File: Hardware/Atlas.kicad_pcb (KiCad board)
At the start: 2 copper layers, 82.5 x 70 mm, 31 parts, among them U1 MS5611, U2 HTU21D, U3 uSD Card, U4 RFD900, U5 MPU9150, U6 XBEE, U7 VENUS838LPX-L

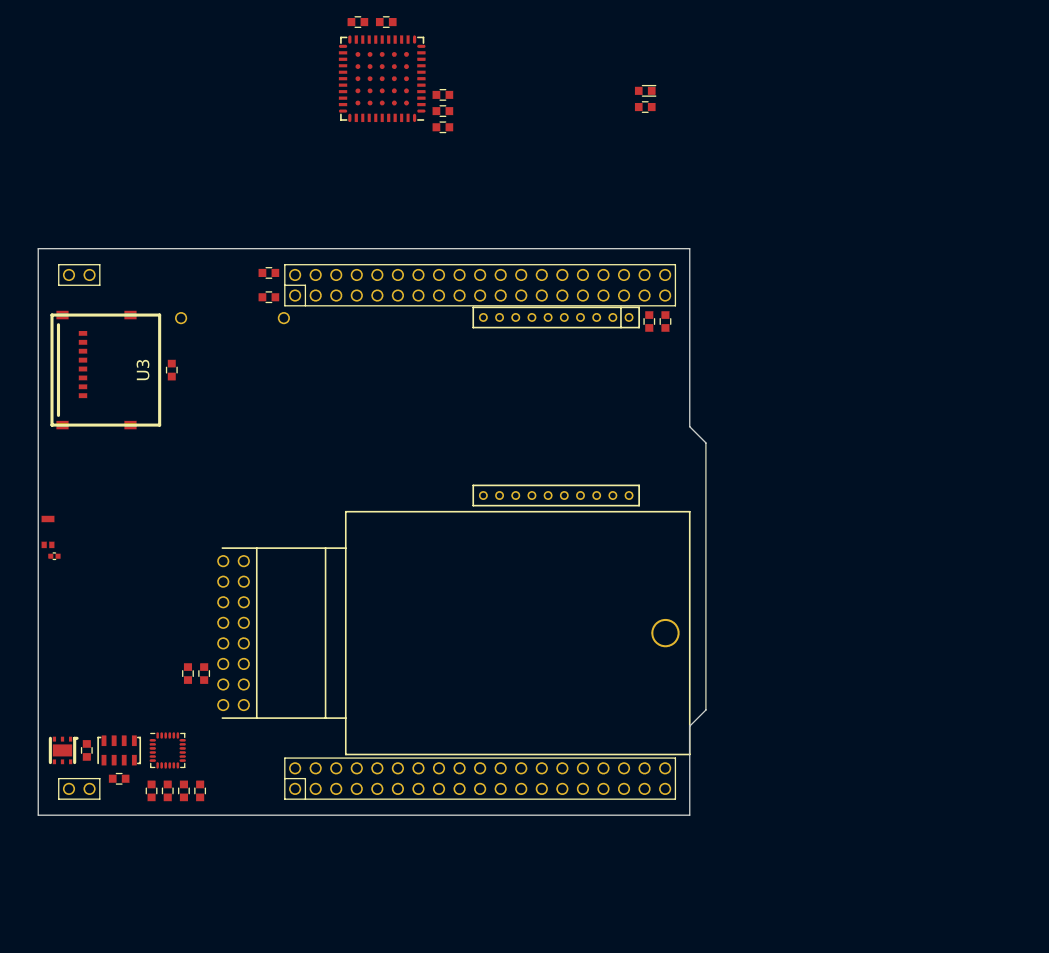
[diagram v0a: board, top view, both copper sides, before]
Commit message: Add 5v regulator and remove before flight switch
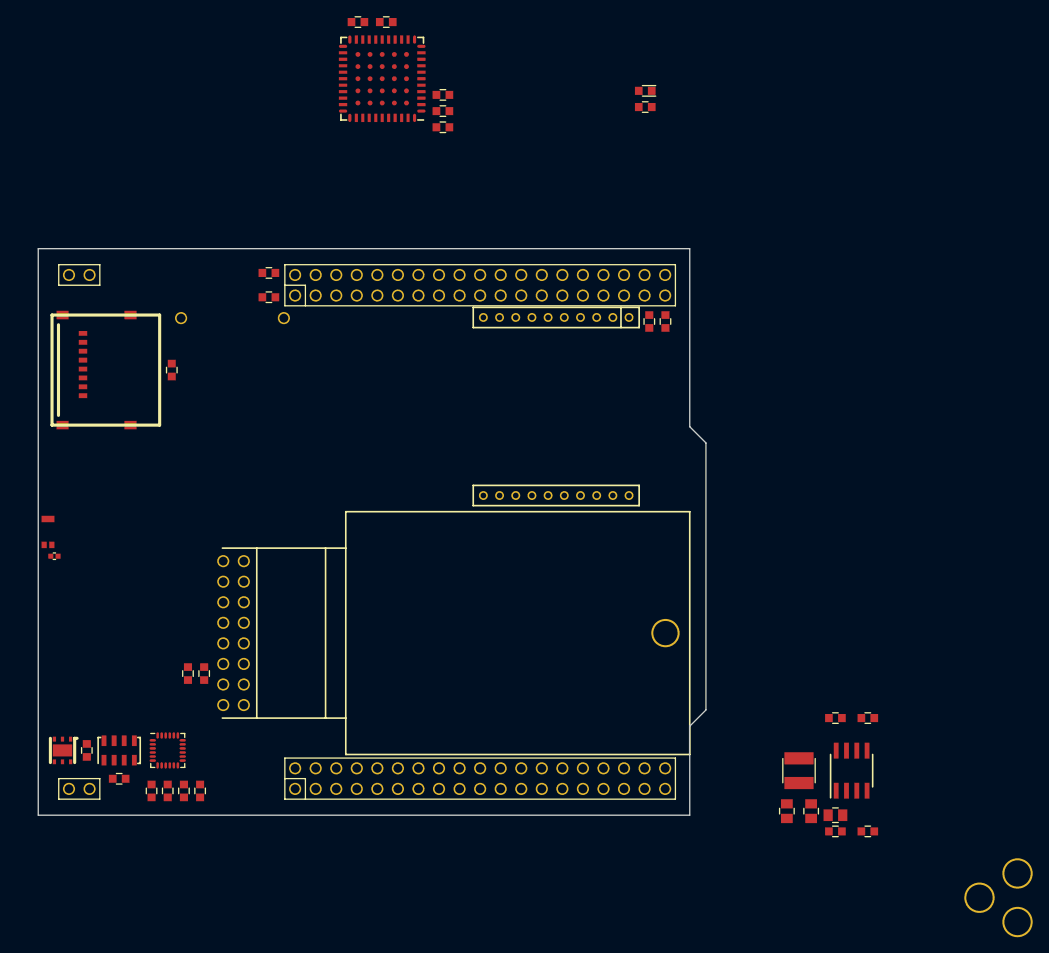
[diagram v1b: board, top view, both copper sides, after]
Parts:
- added C15: 10uF, CAPC2012-N, F.Cu at (198.5, 140.0)
- added C16: C, CAPC1608-N, F.Cu at (198.5, 128.0)
- added C17: 10uF, CAPC2012-N, F.Cu at (195.5, 139.5)
- added C18: 10uF, CAPC2012-N, F.Cu at (192.5, 139.5)
- added J1: DC, CONN-DC-CUI-202, F.Cu at (221.0, 139.5)
- added L2: 4.7uH, INDC-SRN4018, F.Cu at (194.0, 134.5)
- added R6: R, RESC1608-N, F.Cu at (202.5, 128.0)
- added R7: 52.3k, RESC1608-N, F.Cu at (198.5, 142.0)
- added R8: 10k, RESC1608-N, F.Cu at (202.5, 142.0)
- added U8: AOZ1031, SOIC127P600-8N, F.Cu at (200.5, 134.5)
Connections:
- B1 pad 1: (no net) -> +BATT
- B1 pad 2: GND -> N-0000036
- H1 pad D16: (no net) -> +3.3V
- H1 pad D18: (no net) -> +5V
- H1 pad D6: (no net) -> +5V

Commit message: Majority of layout and routing
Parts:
- removed R5: 0, RESC1608-N
- added MECH-HOLE220: VAL**, MECH-HOLE220, F.Cu at (110.0, 137.0)
- added MECH-HOLE220: VAL**, MECH-HOLE220, F.Cu at (110.0, 73.0)
- moved J1 121.5 mm to (100.0, 128.0), turned to 90 degrees
- moved R8 86.3 mm to (117.0, 130.0), turned to 270 degrees
- moved R6 86.0 mm to (117.0, 137.0), turned to 270 degrees
- moved D1 85.2 mm to (98.0, 87.0), turned to 270 degrees
- moved C16 84.0 mm to (115.0, 137.0), turned to 270 degrees
- moved R7 81.9 mm to (117.0, 133.5), turned to 270 degrees
- moved U8 79.5 mm to (121.0, 135.0), turned to 180 degrees
- moved C15 78.2 mm to (121.0, 129.5)
- moved C17 67.5 mm to (128.5, 131.0), turned to 90 degrees
- moved C18 67.5 mm to (125.5, 131.0), turned to 90 degrees
- moved L2 67.0 mm to (127.0, 136.0), turned to 90 degrees
- moved R4 66.3 mm to (122.5, 93.0), turned to 180 degrees
- moved C4 59.9 mm to (107.0, 77.5), turned to 270 degrees
- moved C2 58.5 mm to (127.0, 79.5), turned to 90 degrees
- moved C6 56.6 mm to (107.0, 81.5), turned to 270 degrees
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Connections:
- net N-0000016 renamed /LX
- AE1 pad S: AGND -> GND
- H1 pad D18: +5V -> (no net)
- H1 pad E12: (no net) -> /GOMI
- H1 pad E14: (no net) -> /GIMO
- H1 pad E21: (no net) -> /SIMO
- H1 pad E33: (no net) -> /SOMI
- H1 pad E35: (no net) -> /LIMO
- H1 pad E37: (no net) -> /LOMI
- L1 pad 1: AGND -> GND
- U4 pad 7: (no net) -> /LIMO
- U4 pad 9: (no net) -> /LOMI
- U6 pad 2: (no net) -> /SOMI
- U6 pad 3: (no net) -> /SIMO
- U7 pad 21: AGND -> GND
- U7 pad 22: AGND -> GND
- U7 pad 24: AGND -> GND
- U7 pad 25: AGND -> GND
- U7 pad 27: AGND -> GND
- U7 pad 28: AGND -> GND
- U7 pad 29: AGND -> GND
- U7 pad 31: AGND -> GND
- U7 pad 33: AGND -> GND
- U7 pad 42: (no net) -> /GIMO
- U7 pad 44: (no net) -> /GOMI
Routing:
- net /LIMO: track 0.00 -> 92.8 mm
- net /LOMI: track 0.00 -> 90.9 mm
- net /SCK: track 0.00 -> 77.9 mm
- net /CS: track 0.00 -> 76.6 mm
- net /MOSI: track 0.00 -> 74.6 mm
- net +3.3V: track 0.00 -> 72.7 mm, vias 0 -> 2
- net /MISO: track 0.00 -> 71.5 mm
- net /GIMO: track 0.00 -> 62.8 mm
- net /GOMI: track 0.00 -> 61.0 mm
- net GND: track 0.00 -> 48.9 mm, vias 0 -> 13
- net +5V: track 0.00 -> 42.6 mm
- net +BATT: track 0.00 -> 27.0 mm
- net N-0000035: track 0.00 -> 21.3 mm
- net /SDA: track 0.00 -> 18.4 mm
- net /SCL: track 0.00 -> 17.9 mm
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- added copper zone on F.Cu, net +5V
- added copper zone on F.Cu, net /LX
- added copper zone on F.Cu, net GND
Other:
- board size 82.5 x 70 mm -> 80.5 x 70 mm
- net class Default: clearance 0.254 -> 0.2032; trace_width 0.254 -> 0.2032
- rule trace_clearance: 0.254 -> 0.2032
- rule trace_min: 0.254 -> 0.2032

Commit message: Pre-review layout
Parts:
- moved D1 4.53 mm to (102.5, 86.5), turned to 180 degrees
- moved C1 4.03 mm to (112.0, 79.0)
- moved C2 4.03 mm to (123.0, 79.0)
- moved C4 4.03 mm to (103.0, 77.0)
- moved C5 4.03 mm to (105.5, 83.5)
- moved C6 4.03 mm to (103.0, 81.0)
- moved C7 4.03 mm to (109.5, 83.5)
- moved U1 4.03 mm to (119.5, 79.0)
- moved U2 4.03 mm to (115.0, 79.0)
- moved U5 4.03 mm to (107.5, 79.0)
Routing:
- net /SDA: track 18.4 -> 39.3 mm
- net GND: track 48.9 -> 69.4 mm, vias 13 -> 16
- net /SCL: track 17.9 -> 37.5 mm
- net +3.3V: track 72.7 -> 83.9 mm
- added copper zone on B.Cu, net GND

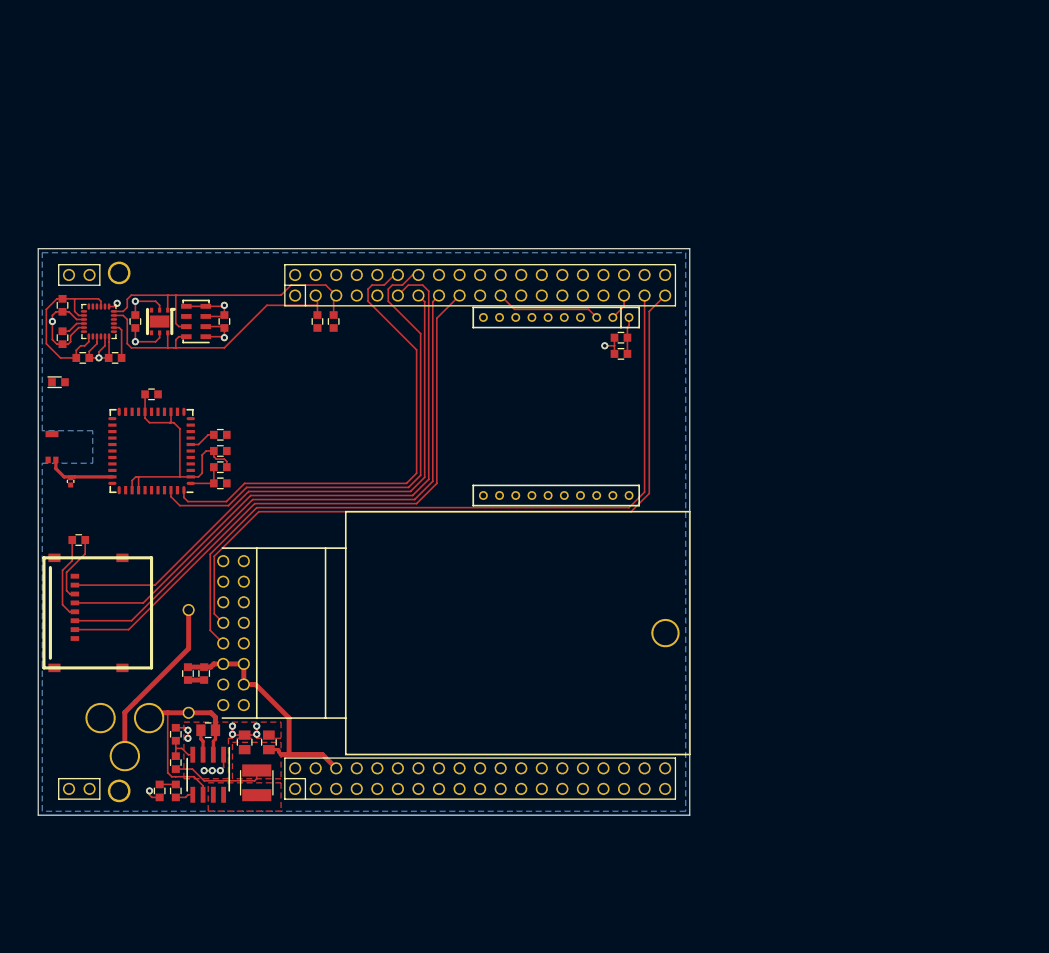
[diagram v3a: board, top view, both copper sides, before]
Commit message: Add LEDs
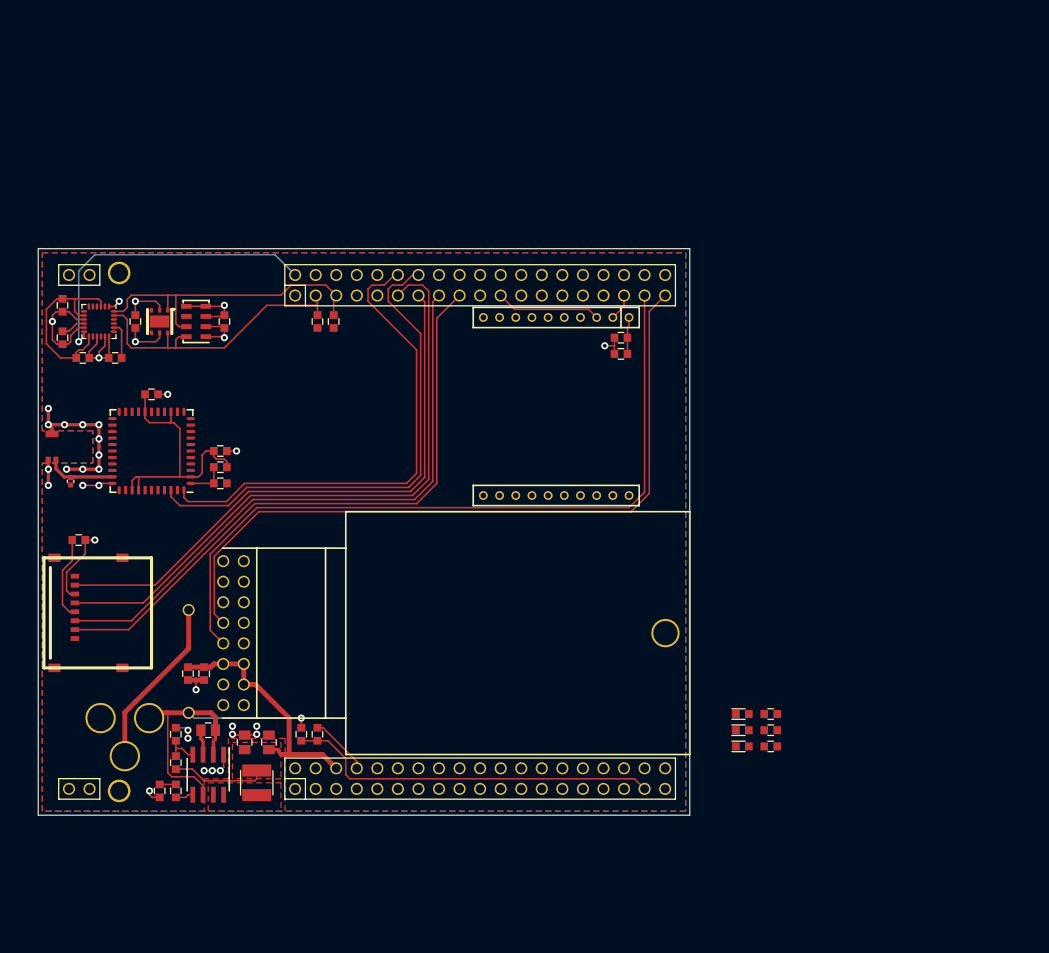
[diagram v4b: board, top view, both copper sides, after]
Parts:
- added D2: LED, LEDC1608-N, F.Cu at (187.0, 129.5)
- added D3: LED, LEDC1608-N, F.Cu at (187.0, 131.5)
- added R10: R, RESC1608-N, F.Cu at (190.5, 129.5)
- added R11: R, RESC1608-N, F.Cu at (190.5, 131.5)
- added R5: R, RESC1608-N, F.Cu at (132.5, 130.0)
- added R9: R, RESC1608-N, F.Cu at (134.5, 130.0)
- moved D1 93.9 mm to (187.0, 127.5)
- moved R4 76.3 mm to (190.5, 127.5), turned to 0 degrees
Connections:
- H1 pad D35: (no net) -> /BattV
- H1 pad E2: (no net) -> /INT
- U5 pad 12: (no net) -> /INT
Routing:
- net /BattV: track 0.00 -> 46.1 mm
- net /INT: track 0.00 -> 38.9 mm, vias 0 -> 1
- net GND: track 69.4 -> 108.0 mm, vias 16 -> 34
- net +BATT: track 27.0 -> 42.4 mm, vias 0 -> 1
- net /NAV: track 3.36 -> 0.00 mm

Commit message: Finish PCB
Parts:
- moved D3 96.0 mm to (102.5, 86.0)
- moved R11 96.0 mm to (106.0, 86.0)
- moved D2 94.1 mm to (102.5, 88.0)
- moved R10 94.1 mm to (106.0, 88.0)
- moved D1 92.4 mm to (102.5, 90.0)
- moved R4 92.4 mm to (106.0, 90.0)
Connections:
- H1 pad E2: /INT -> /LED1
- H1 pad E4: (no net) -> /LED2
- H1 pad E6: (no net) -> /INT
- R10 pad 2: (no net) -> /LED1
- R11 pad 2: (no net) -> /LED2
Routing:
- net +3.3V: track 83.9 -> 395.7 mm, vias 2 -> 6
- net /LED2: track 0.00 -> 40.4 mm, vias 0 -> 1
- net /LED1: track 0.00 -> 38.3 mm, vias 0 -> 1
- net /NAV: track 0.00 -> 21.3 mm
- net /INT: track 38.9 -> 44.5 mm
- net GND: track 108.0 -> 106.1 mm
- net N-0000033: track 0.00 -> 1.90 mm
- net N-0000032: track 0.00 -> 1.90 mm
- net N-000003: track 0.00 -> 1.90 mm

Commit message: Add branding to pcb
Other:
- board text added: "Aerodyne Labs"
- board text added: "Atlas v1.0"
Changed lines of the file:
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@@
     (area 98.610689 69.720599 188.804801 143.2782)
     (thickness 1.6)
-    (drawings 4)
+    (drawings 6)
     (tracks 450)
     (zones 0)
@@
     (18 B.Paste user)
     (19 F.Paste user)
-    (20 B.SilkS user hide)
+    (20 B.SilkS user)
     (21 F.SilkS user hide)
     (22 B.Mask user)
@@
   )
   (setup
-    (last_trace_width 0.4064)
+    (last_trace_width 0.2032)
     (user_trace_width 0.4064)
     (user_trace_width 0.6096)
@@
     (pad_drill 0.6)
     (pad_to_mask_clearance 0)
-    (aux_axis_origin 0 0)
+    (aux_axis_origin 100 140)
     (visible_elements 7FFFFFBF)
     (pcbplotparams
@@
     )
   )
+  (gr_text "Aerodyne Labs" (at 178 78 90) (layer B.SilkS)
+    (effects (font (size 2 2) (thickness 0.3)) (justify left mirror))
+  )
+  (gr_text "Atlas v1.0" (at 175.5 78 90) (layer B.SilkS)
+    (effects (font (size 2 2) (thickness 0.3)) (justify left mirror))
+  )
   (gr_line (start 180.5 70) (end 180.5 140) (angle 90) (layer Edge.Cuts) (width 0.1))

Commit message: DFM changes
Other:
- net class Default: via_drill 0.635 -> 0.508
- rule pad_to_mask_clearance: 0 -> 0.0762
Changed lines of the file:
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@@
     (edge_width 0.1)
     (via_size 0.889)
-    (via_drill 0.635)
+    (via_drill 0.508)
     (via_min_size 0.889)
     (via_min_drill 0.508)
@@
     (mod_text_size 1 1)
     (mod_text_width 0.15)
-    (pad_size 1.5 1.5)
-    (pad_drill 0.6)
-    (pad_to_mask_clearance 0)
+    (pad_size 0.6 1.31)
+    (pad_drill 0)
+    (pad_to_mask_clearance 0.0762)
+    (pad_to_paste_clearance -0.0762)
     (aux_axis_origin 100 140)
     (visible_elements 7FFFFFBF)
     (pcbplotparams
-      (layerselection 3178497)
+      (layerselection 524288)
       (usegerberextensions true)
       (excludeedgelayer true)
@@
       (viasonmask false)
       (mode 1)
-      (useauxorigin false)
+      (useauxorigin true)
       (hpglpennumber 1)
       (hpglpenspeed 20)
@@
       (outputformat 1)
       (mirror false)
-      (drillshape 1)
+      (drillshape 0)
       (scaleselection 1)
-      (outputdirectory ""))
+      (outputdirectory Gerber))
   )
   (net 0 "")
@@
     (trace_width 0.2032)
     (via_dia 0.889)
-    (via_drill 0.635)
+    (via_drill 0.508)
     (uvia_dia 0.508)
     (uvia_drill 0.127)
@@
     )
   )
-  (module SON125P500X300-8N (layer F.Cu)
-    (at 119.5 79 90)
-    (solder_paste_ratio -0.5)
-    (fp_text reference U1 (at 0 -2.9 90) (layer F.SilkS) hide
-      (effects (font (size 1.27 1.27) (thickness 0.254)))
-    )
-    (fp_text value MS5611 (at 0 3.4 90) (layer F.SilkS) hide
-      (effects (font (size 1.524 1.524) (thickness 0.3048)))
-    )
-    (fp_line (start -2.3 -1.6) (end -2.6 -1.6) (layer F.SilkS) (width 0.2032))
-    (fp_line (start -2.6 -1.6) (end -2.6 1.6) (layer F.SilkS) (width 0.2032))
-    (fp_line (start 2.3 -1.6) (end 2.6 -1.6) (layer F.SilkS) (width 0.2032))
-    (fp_line (start 2.6 -1.6) (end 2.6 1.6) (layer F.SilkS) (width 0.2032))
-    (fp_line (start 2.6 1.6) (end 2.3 1.6) (layer F.SilkS) (width 0.2032))
-    (fp_line (start -2.75 -2.11) (end 2.75 -2.11) (layer Eco1.User) (width 0.0762))
-    (fp_line (start 2.75 -2.11) (end 2.75 2.11) (layer Eco1.User) (width 0.0762))
-    (fp_line (start 2.75 2.11) (end -2.75 2.11) (layer Eco1.User) (width 0.0762))
-    (fp_line (start -2.75 2.11) (end -2.75 -2.11) (layer Eco1.User) (width 0.0762))
-    (fp_line (start -2.5 -1.5) (end -2.5 1) (layer Dwgs.User) (width 0.0762))
-    (fp_line (start -2.5 1) (end -2 1.5) (layer Dwgs.User) (width 0.0762))
-    (fp_line (start -2 1.5) (end 2.5 1.5) (layer Dwgs.User) (width 0.0762))
-    (fp_line (start 2.5 1.5) (end 2.5 -1.5) (layer Dwgs.User) (width 0.0762))
-    (fp_line (start 2.5 -1.5) (end -2.5 -1.5) (layer Dwgs.User) (width 0.0762))
-    (pad 1 smd rect (at -1.875 1.2 90) (size 0.6 1.31)
-      (layers F.Cu F.Paste F.Mask)
-      (net 1 +3.3V)
-    )
-    (pad 2 smd rect (at -0.625 1.2 90) (size 0.6 1.31)
-      (layers F.Cu F.Paste F.Mask)
-      (net 1 +3.3V)
-    )
-    (pad 3 smd rect (at 0.625 1.2 90) (size 0.6 1.31)
-      (layers F.Cu F.Paste F.Mask)
-      (net 22 GND)
-    )
-    (pad 4 smd rect (at 1.875 1.2 90) (size 0.6 1.31)
-      (layers F.Cu F.Paste F.Mask)
-      (net 22 GND)
-    )
-    (pad 5 smd rect (at 1.875 -1.2 90) (size 0.6 1.31)
-      (layers F.Cu F.Paste F.Mask)
-      (net 22 GND)
-    )
-    (pad 6 smd rect (at 0.625 -1.2 90) (size 0.6 1.31)
-      (layers F.Cu F.Paste F.Mask)
-    )
-    (pad 7 smd rect (at -0.625 -1.2 90) (size 0.6 1.31)
-      (layers F.Cu F.Paste F.Mask)
-      (net 19 /SDA)
-    )
-    (pad 8 smd rect (at -1.875 -1.2 90) (size 0.6 1.31)
-      (layers F.Cu F.Paste F.Mask)
-      (net 18 /SCL)
-    )
-    (model 3D\Misc\MS5611.wrl
-      (at (xyz 0 0 0))
-      (scale (xyz 0.393701 0.393701 0.393701))
-      (rotate (xyz 0 0 0))
-    )
-  )
   (module SON100P300X300X110-7N (layer F.Cu)
     (at 115 79 180)
@@
       (at (xyz 0 0 0))
       (scale (xyz 0.393701 0.393701 0.393701))
+      (rotate (xyz 0 0 0))
+    )
+  )
+  (module SON125P500X300-8N (layer F.Cu)
+    (at 119.5 79 90)
+    (fp_text reference U1 (at 0 -2.9 90) (layer F.SilkS) hide
+      (effects (font (size 1.27 1.27) (thickness 0.254)))
+    )
+    (fp_text value MS5611 (at 0 3.4 90) (layer F.SilkS) hide
+      (effects (font (size 1.524 1.524) (thickness 0.3048)))
+    )
+    (fp_line (start -2.3 -1.6) (end -2.6 -1.6) (layer F.SilkS) (width 0.2032))
+    (fp_line (start -2.6 -1.6) (end -2.6 1.6) (layer F.SilkS) (width 0.2032))
+    (fp_line (start 2.3 -1.6) (end 2.6 -1.6) (layer F.SilkS) (width 0.2032))
+    (fp_line (start 2.6 -1.6) (end 2.6 1.6) (layer F.SilkS) (width 0.2032))
+    (fp_line (start 2.6 1.6) (end 2.3 1.6) (layer F.SilkS) (width 0.2032))
+    (fp_line (start -2.75 -2.11) (end 2.75 -2.11) (layer Eco1.User) (width 0.0762))
+    (fp_line (start 2.75 -2.11) (end 2.75 2.11) (layer Eco1.User) (width 0.0762))
+    (fp_line (start 2.75 2.11) (end -2.75 2.11) (layer Eco1.User) (width 0.0762))
+    (fp_line (start -2.75 2.11) (end -2.75 -2.11) (layer Eco1.User) (width 0.0762))
+    (fp_line (start -2.5 -1.5) (end -2.5 1) (layer Dwgs.User) (width 0.0762))
+    (fp_line (start -2.5 1) (end -2 1.5) (layer Dwgs.User) (width 0.0762))
+    (fp_line (start -2 1.5) (end 2.5 1.5) (layer Dwgs.User) (width 0.0762))
+    (fp_line (start 2.5 1.5) (end 2.5 -1.5) (layer Dwgs.User) (width 0.0762))
+    (fp_line (start 2.5 -1.5) (end -2.5 -1.5) (layer Dwgs.User) (width 0.0762))
+    (pad 1 smd rect (at -1.875 1.2 90) (size 0.6 1.31)
+      (layers F.Cu F.Paste F.Mask)
+      (net 1 +3.3V)
+    )
+    (pad 2 smd rect (at -0.625 1.2 90) (size 0.6 1.31)
+      (layers F.Cu F.Paste F.Mask)
+      (net 1 +3.3V)
+    )
+    (pad 3 smd rect (at 0.625 1.2 90) (size 0.6 1.31)
+      (layers F.Cu F.Paste F.Mask)
+      (net 22 GND)
+    )
+    (pad 4 smd rect (at 1.875 1.2 90) (size 0.6 1.31)
+      (layers F.Cu F.Paste F.Mask)
+      (net 22 GND)
+    )
+    (pad 5 smd rect (at 1.875 -1.2 90) (size 0.6 1.31)
+      (layers F.Cu F.Paste F.Mask)
+      (net 22 GND)
+    )
+    (pad 6 smd rect (at 0.625 -1.2 90) (size 0.6 1.31)
+      (layers F.Cu F.Paste F.Mask)
+    )
+    (pad 7 smd rect (at -0.625 -1.2 90) (size 0.6 1.31)
+      (layers F.Cu F.Paste F.Mask)
+      (net 19 /SDA)
+    )
+    (pad 8 smd rect (at -1.875 -1.2 90) (size 0.6 1.31)
+      (layers F.Cu F.Paste F.Mask)
+      (net 18 /SCL)
+    )
+    (model 3D\Misc\MS5611.wrl
+      (at (xyz 0 0 0))
+      (scale (xyz 0.393701 0.393701 0.393701))
